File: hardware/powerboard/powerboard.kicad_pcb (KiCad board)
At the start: 4 copper layers, 81.2 x 50.7 mm, 70 parts, among them J1 USB_B_Micro, J10 5V, J11 3V3, J2 Boot, J3 Power, J4 Display, J5 Debug, J6 SPI_1, J7 UART_0, J8 I2C_0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

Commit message: More powerboard finalization
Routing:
- net GND: vias 87 -> 88
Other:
- board text added: "Boot"
- board text added: "Landyn Francis Jacob Mealey"
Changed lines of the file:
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@@
     (property "Sheetname" "")
     (attr through_hole)
-    (fp_text reference "J2" (at -0.127 5.593 -90 unlocked) (layer "F.SilkS")
+    (fp_text reference "J2" (at -0.2794 -2.6162 unlocked) (layer "F.SilkS")
       (effects (font (size 1 1) (thickness 0.15)))
     )
@@
     (effects (font (size 1 1) (thickness 0.15)))
   )
+  (gr_text "Landyn Francis\nJacob Mealey" (at 103.6828 61.6712) (layer "F.SilkS")
+    (effects (font (size 1 1) (thickness 0.2)))
+  )
   (gr_text "TX_0\n" (at 90.4494 62.223638 270) (layer "F.SilkS")
     (effects (font (size 1 1) (thickness 0.15)))
@@
     (effects (font (size 1 1) (thickness 0.15)))
   )
+  (gr_text "GND" (at 77.9018 62.3316 270) (layer "F.SilkS")
+    (effects (font (size 1 1) (thickness 0.15)))
+  )
+  (gr_text "GND" (at 87.7824 62.3316 270) (layer "F.SilkS")
+    (effects (font (size 1 1) (thickness 0.15)))
+  )
   (gr_text "SDA_1" (at 96.527858 55.9054) (layer "F.SilkS")
+    (effects (font (size 1 1) (thickness 0.15)))
+  )
+  (gr_text "Boot" (at 66.5988 18.7198) (layer "F.SilkS")
     (effects (font (size 1 1) (thickness 0.15)))
   )
@@
   (via (at 116.2558 45.212) (size 0.8) (drill 0.3) (layers "F.Cu" "B.Cu") (free) (net 1))
   (via (at 58.2676 44.6024) (size 0.8) (drill 0.3) (layers "F.Cu" "B.Cu") (free) (net 1))
-  (via (at 74.2696 31.6875) (size 0.8) (drill 0.3) (layers "F.Cu" "B.Cu") (free) (net 1))
   (via (at 88.1888 50.9016) (size 0.8) (drill 0.3) (layers "F.Cu" "B.Cu") (free) (net 1))
   (via (at 89.5604 34.6964) (size 0.8) (drill 0.3) (layers "F.Cu" "B.Cu") (free) (net 1))
@@
   (via (at 68.3006 59.8678) (size 0.8) (drill 0.3) (layers "F.Cu" "B.Cu") (free) (net 1))
   (via (at 93.1672 43.5102) (size 0.8) (drill 0.3) (layers "F.Cu" "B.Cu") (free) (net 1))
+  (via (at 82.5246 50.6984) (size 0.8) (drill 0.3) (layers "F.Cu" "B.Cu") (free) (net 1))
   (via (at 91.4654 34.6964) (size 0.8) (drill 0.3) (layers "F.Cu" "B.Cu") (free) (net 1))
   (via (at 105.0544 19.5834) (size 0.8) (drill 0.3) (layers "F.Cu" "B.Cu") (free) (net 1))
   (via (at 72.263 50.2412) (size 0.8) (drill 0.3) (layers "F.Cu" "B.Cu") (net 1))
-  (via (at 73.9902 30.1498) (size 0.8) (drill 0.3) (layers "F.Cu" "B.Cu") (free) (net 1))
+  (via (at 74.9554 29.8196) (size 0.8) (drill 0.3) (layers "F.Cu" "B.Cu") (free) (net 1))
   (via (at 115.951 37.8968) (size 0.8) (drill 0.3) (layers "F.Cu" "B.Cu") (free) (net 1))
   (via (at 95.0722 43.5102) (size 0.8) (drill 0.3) (layers "F.Cu" "B.Cu") (free) (net 1))
@@
   (via (at 109.728 17.145) (size 0.8) (drill 0.3) (layers "F.Cu" "B.Cu") (free) (net 1))
   (via (at 127.9652 22.606) (size 0.8) (drill 0.3) (layers "F.Cu" "B.Cu") (free) (net 1))
+  (via (at 82.5246 52.3494) (size 0.8) (drill 0.3) (layers "F.Cu" "B.Cu") (free) (net 1))
   (via (at 103.029653 64.6176) (size 0.8) (drill 0.3) (layers "F.Cu" "B.Cu") (free) (net 1))
   (via (at 78.3844 46.5836) (size 0.8) (drill 0.3) (layers "F.Cu" "B.Cu") (free) (net 1))
@@
   (segment (start 75.9144 36.40815) (end 75.9144 36.0236) (width 0.2) (layer "F.Cu") (net 2))
   (segment (start 107.1118 30.5562) (end 107.1118 29.273) (width 0.2) (layer "F.Cu") (net 2))
+  (segment (start 76.3144 32.166583) (end 76.3144 35.6236) (width 0.2) (layer "F.Cu") (net 2))
   (segment (start 81.0514 37.1094) (end 80.91515 37.24565) (width 0.2) (layer "F.Cu") (net 2))
   (segment (start 74.295 28.7274) (end 74.2696 28.7528) (width 0.2) (layer "F.Cu") (net 2))
@@
   (segment (start 75.9144 45.777) (end 75.9144 43.28315) (width 0.2) (layer "F.Cu") (net 2))
   (segment (start 70.96515 40.84565) (end 72.2769 40.84565) (width 0.2) (layer "F.Cu") (net 2))
-  (segment (start 75.4126 31.264783) (end 76.3144 32.166583) (width 0.2) (layer "F.Cu") (net 2))
-  (segment (start 75.4126 30.988) (end 75.4126 31.264783) (width 0.2) (layer "F.Cu") (net 2))
+  (segment (start 74.549 31.1658) (end 75.313617 31.1658) (width 0.2) (layer "F.Cu") (net 2))
   (segment (start 79.1464 35.2806) (end 80.0862 35.2806) (width 0.2) (layer "F.Cu") (net 2))
   (segment (start 113.2078 59.309) (end 114.9964 59.309) (width 0.2) (layer "F.Cu") (net 2))
@@
   (segment (start 78.3144 36.40815) (end 78.3144 36.0364) (width 0.2) (layer "F.Cu") (net 2))
   (segment (start 75.2348 46.4566) (end 75.9144 45.777) (width 0.2) (layer "F.Cu") (net 2))
+  (segment (start 75.313617 31.1658) (end 76.3144 32.166583) (width 0.2) (layer "F.Cu") (net 2))
   (segment (start 78.5622 35.7886) (end 79.8068 35.7886) (width 0.2) (layer "F.Cu") (net 2))
   (segment (start 113.8052 43.942) (end 115.1006 42.6466) (width 0.2) (layer "F.Cu") (net 2))
   (segment (start 80.0862 35.5092) (end 80.0862 35.2806) (width 0.2) (layer "F.Cu") (net 2))
-  (segment (start 76.3144 32.166583) (end 76.3144 35.6236) (width 0.2) (layer "F.Cu") (net 2))
   (segment (start 78.3144 36.0364) (end 78.5622 35.7886) (width 0.2) (layer "F.Cu") (net 2))
   (segment (start 74.2696 28.7528) (end 71.3904 28.7528) (width 0.2) (layer "F.Cu") (net 2))
@@
   (via (at 113.538 43.942) (size 0.8) (drill 0.3) (layers "F.Cu" "B.Cu") (free) (net 2))
   (via (at 98.044 19.2024) (size 0.8) (drill 0.3) (layers "F.Cu" "B.Cu") (free) (net 2))
-  (via (at 75.4126 30.988) (size 0.8) (drill 0.3) (layers "F.Cu" "B.Cu") (free) (net 2))
+  (via (at 74.549 31.1658) (size 0.8) (drill 0.3) (layers "F.Cu" "B.Cu") (free) (net 2))
   (via (at 58.2422 25.781) (size 0.8) (drill 0.3) (layers "F.Cu" "B.Cu") (net 2))
   (segment (start 72.2604 36.5506) (end 73.152 37.4422) (width 0.2) (layer "B.Cu") (net 2))
   (segment (start 75.5396 46.1518) (end 75.5396 42.6948) (width 0.2) (layer "B.Cu") (net 2))
-  (segment (start 76.2139 36.9203) (end 76.2 36.9342) (width 0.2) (layer "B.Cu") (net 2))
+  (segment (start 74.549 31.1658) (end 73.73685 31.1658) (width 0.2) (layer "B.Cu") (net 2))
   (segment (start 83.7184 40.8432) (end 78.8136 40.8432) (width 0.2) (layer "B.Cu") (net 2))
-  (segment (start 75.4126 30.988) (end 73.91465 30.988) (width 0.2) (layer "B.Cu") (net 2))
   (segment (start 81.0514 37.1094) (end 81.0514 37.5894) (width 0.2) (layer "B.Cu") (net 2))
+  (segment (start 73.214 31.68865) (end 73.214 36.0056) (width 0.2) (layer "B.Cu") (net 2))
   (segment (start 70.6628 36.5506) (end 72.2604 36.5506) (width 0.2) (layer "B.Cu") (net 2))
   (segment (start 78.1812 36.195) (end 78.1812 36.9088) (width 0.2) (layer "B.Cu") (net 2))
-  (segment (start 73.91465 30.988) (end 73.214 31.68865) (width 0.2) (layer "B.Cu") (net 2))
   (segment (start 80.0862 35.2806) (end 80.0862 37.5386) (width 0.2) (layer "B.Cu") (net 2))
   (segment (start 70.9676 40.8432) (end 72.8498 40.8432) (width 0.2) (layer "B.Cu") (net 2))
   (segment (start 81.0514 37.5894) (end 78.7374 39.9034) (width 0.2) (layer "B.Cu") (net 2))
-  (segment (start 75.4126 30.988) (end 76.2139 31.7893) (width 0.2) (layer "B.Cu") (net 2))
+  (segment (start 73.73685 31.1658) (end 73.214 31.68865) (width 0.2) (layer "B.Cu") (net 2))
+  (segment (start 76.2139 36.9203) (end 76.2 36.9342) (width 0.2) (layer "B.Cu") (net 2))
+  (segment (start 76.2139 32.8307) (end 76.2139 36.9203) (width 0.2) (layer "B.Cu") (net 2))
   (segment (start 80.0862 37.5386) (end 78.7374 38.8874) (width 0.2) (layer "B.Cu") (net 2))
+  (segment (start 73.214 36.0056) (end 74.1426 36.9342) (width 0.2) (layer "B.Cu") (net 2))
   (segment (start 70.1802 41.6306) (end 70.9676 40.8432) (width 0.2) (layer "B.Cu") (net 2))
-  (segment (start 76.2139 31.7893) (end 76.2139 36.9203) (width 0.2) (layer "B.Cu") (net 2))
   (segment (start 79.121 35.2552) (end 80.0608 35.2552) (width 0.2) (layer "B.Cu") (net 2))
   (segment (start 80.0608 35.2552) (end 80.0862 35.2806) (width 0.2) (layer "B.Cu") (net 2))
   (segment (start 79.121 35.2552) (end 78.1812 36.195) (width 0.2) (layer "B.Cu") (net 2))
   (segment (start 84.1502 40.4114) (end 83.7184 40.8432) (width 0.2) (layer "B.Cu") (net 2))
-  (segment (start 73.214 36.0056) (end 74.1426 36.9342) (width 0.2) (layer "B.Cu") (net 2))
   (segment (start 75.2348 46.4566) (end 75.5396 46.1518) (width 0.2) (layer "B.Cu") (net 2))
-  (segment (start 73.214 31.68865) (end 73.214 36.0056) (width 0.2) (layer "B.Cu") (net 2))
+  (segment (start 74.549 31.1658) (end 76.2139 32.8307) (width 0.2) (layer "B.Cu") (net 2))
   (segment (start 77.6478 37.4613) (end 77.33215 37.14565) (width 0.2) (layer "F.Cu") (net 3))
   (segment (start 77.33215 37.14565) (end 77.5144 36.9634) (width 0.2) (layer "F.Cu") (net 3))
@@
     (connect_pads (clearance 0))
     (min_thickness 0.254)
-    (keepout (tracks not_allowed) (vias not_allowed) (pads not_allowed) (copperpour not_allowed) (footprints allowed))
+    (keepout (tracks not_allowed) (vias not_allowed) (pads not_allowed ) (copperpour not_allowed) (footprints allowed))
     (fill (thermal_gap 0.508) (thermal_bridge_width 0.508))
     (polygon

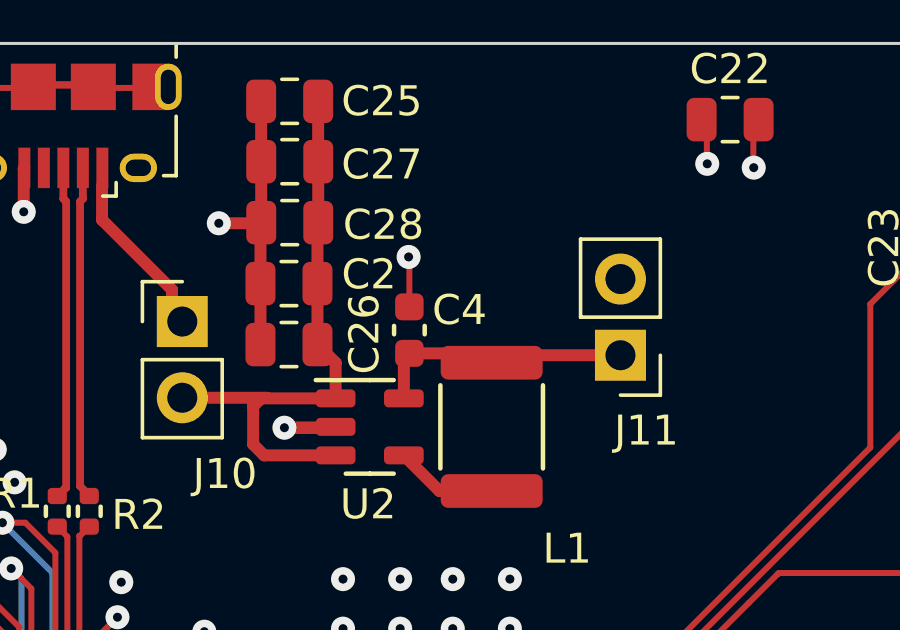
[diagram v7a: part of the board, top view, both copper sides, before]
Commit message: MIDI Messages now only sent on Keypress
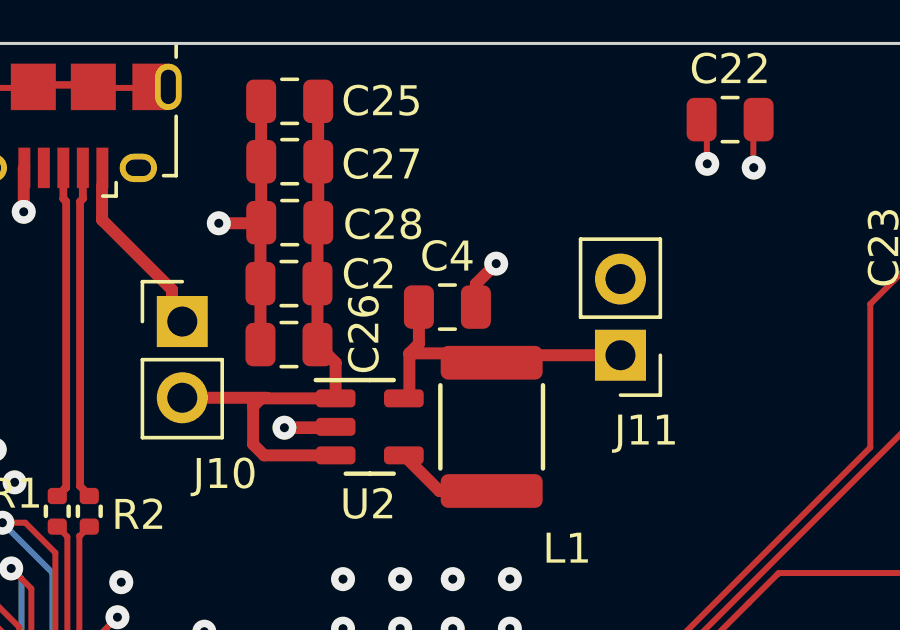
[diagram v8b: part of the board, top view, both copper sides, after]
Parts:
- C4: footprint Capacitor_SMD:C_0603_1608Metric -> Capacitor_SMD:C_0805_2012Metric
- moved C4 1.48 mm to (89.4, 24.0), turned to 0 degrees
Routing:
- net Net-(C4-Pad1): track 8.85 -> 10.5 mm
